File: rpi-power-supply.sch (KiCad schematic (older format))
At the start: 25 parts, among them IC1 ATTINY85-P, IC2 STEP_DOWN_CONVERTER_(MP2307), P1 CONN_01X03, P2 CONN_01X02, Q1 MOSFET_N_(2N7002P,215), U1 LM3480-3.3

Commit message: - Finished schematic.
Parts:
- removed CONN_1: CONN_02X10, rpi-shutdown-pcb:HEADER_20_PIN_FEMALE_(PPTC102LFBN-RC), symbol CONN_02X10
- removed IC1: ATTINY85-P, Housings_DIP:DIP-8_W7.62mm, symbol ATTINY85-P
- removed P1: CONN_01X03, rpi-shutdown-pcb:3_PADS_FOR_18_AWG_WIRE, symbol CONN_01X03
- removed P2: CONN_01X02, rpi-shutdown-pcb:2_PADS_FOR_18_AWG_WIRE, symbol CONN_01X02
- added 5V_1, GND_1, GND_2, IGN_1, VBATT_1: CONN_01X01, rpi-power-supply:2mm_X_3mm_WIRE_PAD, symbol CONN_01X01
- added CONN_1: Raspberry_Pi_2_3, Pin_Headers:Pin_Header_Straight_2x20_Pitch2.54mm_SMD, symbol Raspberry_Pi_2_3
- added IC1: ATTINY85-20SU, rpi-power-supply:SOIC-8_WIDE_Pitch1.27mm, symbol ATTINY85-20SU
- added ICSP_1: CONN_02X03, Pin_Headers:Pin_Header_Straight_2x03_Pitch2.54mm_SMD, symbol CONN_02X03
- added R9: 1K, Resistors_SMD:R_0805, symbol R
- C1, C2: footprint rpi-shutdown-pcb:R_1206_HandSoldering_(narrow) -> Capacitors_SMD:C_0805
- C3, C4, C7: footprint rpi-shutdown-pcb:R_1206_HandSoldering_(narrow) -> Capacitors_SMD:C_1206
- C5, C6: footprint rpi-shutdown-pcb:C_0805_HandSoldering_(narrow) -> Capacitors_SMD:C_0805
- D1: footprint rpi-shutdown-pcb:DO-214AB -> rpi-power-supply:DO-214AB
- F1: footprint rpi-shutdown-pcb:R_1812_HandSoldering -> Resistors_SMD:R_1812
- IC2: footprint rpi-shutdown-pcb:SOIC8N_(EXPOSED_PAD) -> rpi-power-supply:SOIC8N_(EXPOSED_PAD)
- L1: footprint rpi-shutdown-pcb:INDUCTOR_10uH_(ASPI-0630LR) -> rpi-power-supply:INDUCTOR_10uH_(ASPI-0630LR)
- Q1, U1: footprint TO_SOT_Packages_SMD:SOT-23_Handsoldering -> TO_SOT_Packages_SMD:SOT-23
- R1, R2, R3, R4, R5, R6, R7, R8: footprint rpi-shutdown-pcb:R_1206_HandSoldering_(narrow) -> Resistors_SMD:R_0805
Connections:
- net GND: now also CONN_1.14 (GND), CONN_1.20 (GND), CONN_1.25 (GND), CONN_1.30 (GND), CONN_1.34 (GND), CONN_1.39 (GND), CONN_1.6 (GND), CONN_1.9 (GND), GND_1.1 (P1), GND_2.1 (P1), IC1.4 (GND), ICSP_1.6 (P6)
- net MOSI: now reaches Q1.3 (D), R3.2
- net MOSI: now also IC1.5 (PB0(MOSI/DI/SDA/AIN0/OC0A/~OC1A~/AREF/PCINT0)), ICSP_1.4 (P4)
- net MISO: now reaches IC2.7 (EN), R4.1
- net MISO: now also IC1.6 (PB1(MISO/DO/AIN1/OC0B/OC1A/PCINT1)), ICSP_1.1 (P1)
- net SCK: now reaches R6.1
- net SCK: now also CONN_1.11 (GPIO17_(GEN0)), IC1.7 (PB2(SCK/USCK/SCL/T0/INT0/ADC1/PCINT2)), ICSP_1.3 (P3)
- net 3.3V: now reaches C2.1, R3.1, U1.1 (VOUT)
- net 3.3V: now also IC1.8 (VCC), ICSP_1.2 (P2), R9.1
- net 5V: now reaches C7.1, L1.2, R8.1
- net 5V: now also 5V_1.1 (P1), CONN_1.2 (5V), CONN_1.4 (5V)
- net at R1.1, R2.2: now also IGN_1.1 (P1)
- net at D1.2 (A): now also VBATT_1.1 (P1)
- new net PI_3.3V: CONN_1.1 (3V3), CONN_1.17 (3V3)
- new net PI_INT: CONN_1.22 (GPIO25_(GEN6))
- new net PI_MISO: CONN_1.21 ((SPI_MISO)_GPIO9)
- new net PI_MOSI: CONN_1.19 ((SPI_MOSI)_GPIO10)
- new net PI_SCK: CONN_1.23 ((SPI_SCLK)_GPIO11)
- new net PI_SCL: CONN_1.5 ((SCL1)_GPIO3)
- new net PI_SDA: CONN_1.3 ((SDA1)_GPIO2)
- new net PI_SS: CONN_1.24 ((~SPI_CE0~)_GPIO8)
- new net RST: IC1.1 (PB5(~RESET~/dW/ADC0/PCINT5)), ICSP_1.5 (P5), R9.2
- no-connect marks 4 -> 23
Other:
- note removed: "+5V"
- note removed: "GND"
- note removed: "GPIO17"
- note removed: "IGN"
- note removed: "Vbatt"
- note removed: "Vout+"
- note removed: "Vout-"
- moved on the sheet: C1, C2, C3, C4, C5, C6, C7, D1, F1, IC2, L1, Q1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

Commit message: - Started on PCB layout.
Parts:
- CONN_1: footprint Pin_Headers:Pin_Header_Straight_2x20_Pitch2.54mm_SMD -> rpi-power-supply:Pin_Header_Straight_2x20_Pitch2.54mm_SMD_(mirrored)
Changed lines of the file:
@@
 F 0 "CONN_1" H 10250 2750 50  0000 C CNN
 F 1 "Raspberry_Pi_2_3" H 9150 4900 50  0000 C CNN
-F 2 "Pin_Headers:Pin_Header_Straight_2x20_Pitch2.54mm_SMD" H 10550 5250 50  0001 C CNN
+F 2 "rpi-power-supply:Pin_Header_Straight_2x20_Pitch2.54mm_SMD_(mirrored)" H 10550 5250 50  0001 C CNN
 F 3 "" H 9600 3850 50  0001 C CNN
 	1    9550 4000

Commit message: - Finished PCB design.
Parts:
- CONN_1: footprint rpi-power-supply:Pin_Header_Straight_2x20_Pitch2.54mm_SMD_(mirrored) -> rpi-power-supply:40-PIN_SMD_(M20-7812045)
- ICSP_1: footprint Pin_Headers:Pin_Header_Straight_2x03_Pitch2.54mm_SMD -> rpi-power-supply:2X3_HEADER_SMD_HORIZONTAL
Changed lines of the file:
@@
 F 0 "CONN_1" H 10250 2750 50  0000 C CNN
 F 1 "Raspberry_Pi_2_3" H 9150 4900 50  0000 C CNN
-F 2 "rpi-power-supply:Pin_Header_Straight_2x20_Pitch2.54mm_SMD_(mirrored)" H 10550 5250 50  0001 C CNN
+F 2 "rpi-power-supply:40-PIN_SMD_(M20-7812045)" H 10550 5250 50  0001 C CNN
 F 3 "" H 9600 3850 50  0001 C CNN
 	1    9550 4000
@@
 F 0 "ICSP_1" H 1550 6900 50  0000 C CNN
 F 1 "CONN_02X03" H 1550 6500 50  0001 C CNN
-F 2 "Pin_Headers:Pin_Header_Straight_2x03_Pitch2.54mm_SMD" H 1550 5500 50  0001 C CNN
+F 2 "rpi-power-supply:2X3_HEADER_SMD_HORIZONTAL" H 1550 5500 50  0001 C CNN
 F 3 "" H 1550 5500 50  0001 C CNN
 	1    1550 6700

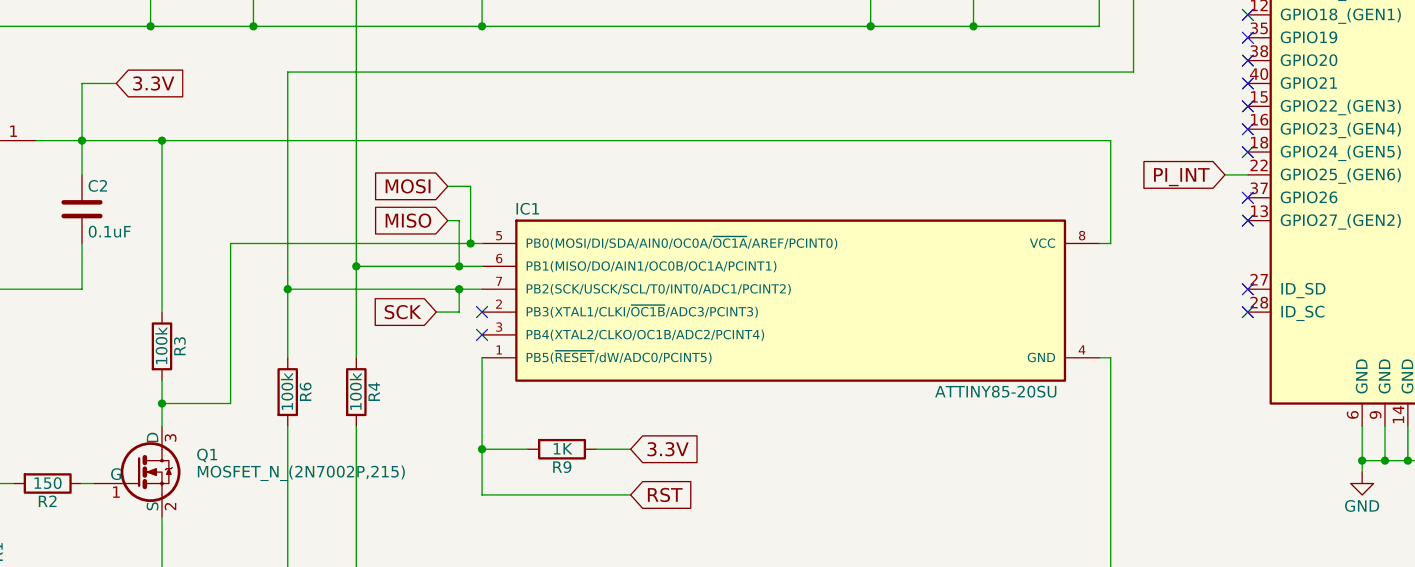
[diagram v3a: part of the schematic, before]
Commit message: - Added connection from ignition input to RPi input.
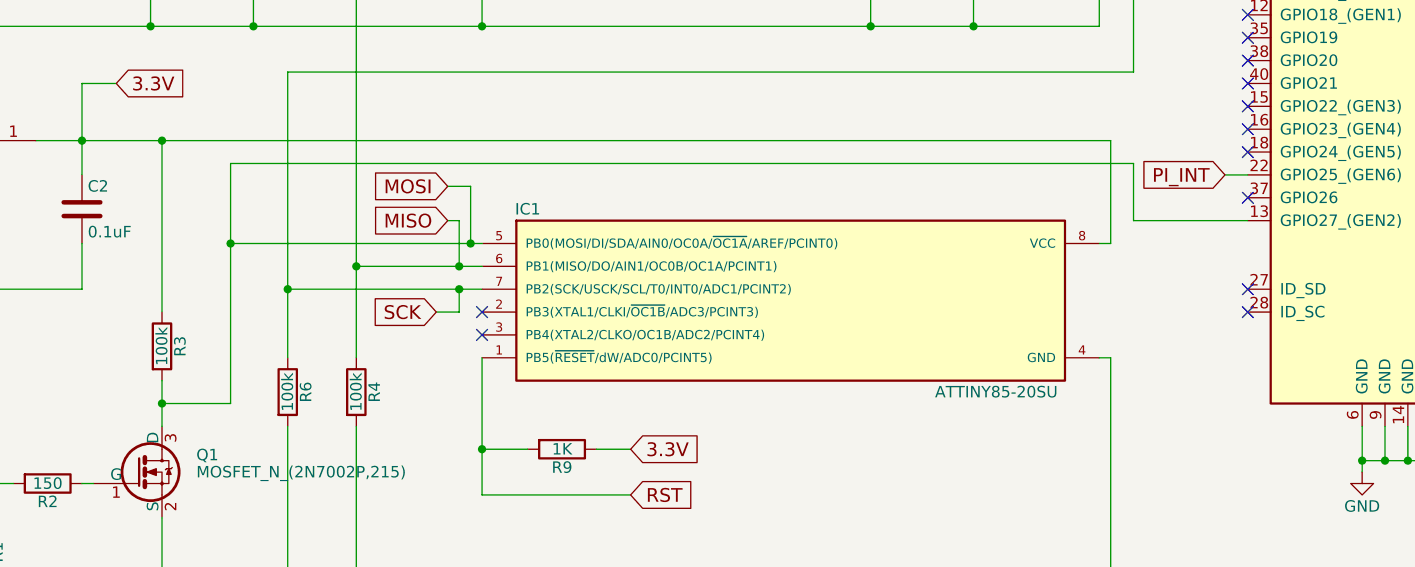
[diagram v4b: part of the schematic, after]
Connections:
- net MOSI: now also CONN_1.13 (GPIO27_(GEN2))
- no-connect marks 23 -> 22
